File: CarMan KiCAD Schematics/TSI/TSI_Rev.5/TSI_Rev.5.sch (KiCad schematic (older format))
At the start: 24 parts, among them J25 Current_Sensor, J26 Conn_02x12_Counter_Clockwise

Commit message: TSI J13 & TSI J14
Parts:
- removed J?: J14, symbol Connector_Generic:Conn_01x04
- removed J?: J13, symbol Connector_Generic:Conn_01x04
- added J?: J14, symbol Connector_Generic:Conn_01x06
- added J?: J13, symbol Connector_Generic:Conn_01x02
- J?: value TSI J2 -> J2
- J?: value TSI J3 -> J3
- J?: value TSI J4 -> J4
- J?: value TSI J5 -> J5
- J?: value TSI J6 -> J6
- J?: value TSI J8 -> J8
- J?: value TSI J9 -> J9
- J?: value TSI J7 -> J7
- J?: value TSI J32 -> J32
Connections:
- net AMS_FAULT_LED: now also J?.1 (Pin_1)
- net FAULT_LED_RTN: now also J?.2 (Pin_2), J?.3 (Pin_3)
- net IMD_FAULT_LED: now also J?.4 (Pin_4)
- net TSAL: now also J?.1 (Pin_1)
- net TSAL_Cockpit: now also J?.5 (Pin_5)
- net TSAL_RTN: now also J?.2 (Pin_2), J?.6 (Pin_6)
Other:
- note added: "TSAL Roll \nHoop Power\n"
- note removed: "TSAL Power"
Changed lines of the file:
@@
 Text Label 9450 900  2    50   ~ 0
 AIRS
-Text Notes 7750 2100 0    50   ~ 0
+Text Notes 7800 2350 0    50   ~ 0
 Dashboard\n
-Text Label 7800 1650 2    50   ~ 0
-AMS_FAULT_LED
-Text Label 7800 1750 2    50   ~ 0
-FAULT_LED_RTN
-Text Label 7800 1950 2    50   ~ 0
-IMD_FAULT_LED
-Text Label 7800 1850 2    50   ~ 0
-FAULT_LED_RTN
 Text Notes 2450 1150 0    50   ~ 0
 Precharge Relay\n\n\n
@@
 Text Label 2500 1700 2    50   ~ 0
 GLV_RTN
-Text Notes 6750 2100 0    50   ~ 0
-TSAL Power
 Wire Wire Line
 	2750 4100 2850 4100
@@
 P 6000 900
 F 0 "J?" H 6080 892 50  0001 L CNN
-F 1 "TSI J2" H 5900 1250 50  0000 L CNN
+F 1 "J2" H 5950 1200 50  0000 L CNN
 F 2 "" H 6000 900 50  0001 C CNN
 F 3 "~" H 6000 900 50  0001 C CNN
@@
 P 6850 900
 F 0 "J?" H 6930 892 50  0001 L CNN
-F 1 "TSI J3" H 6750 1250 50  0000 L CNN
+F 1 "J3" H 6800 1200 50  0000 L CNN
 F 2 "" H 6850 900 50  0001 C CNN
 F 3 "~" H 6850 900 50  0001 C CNN
@@
 P 8950 900
 F 0 "J?" H 9030 892 50  0001 L CNN
-F 1 "TSI J5" H 8850 1250 50  0000 L CNN
+F 1 "J5" H 8900 1200 50  0000 L CNN
 F 2 "" H 8950 900 50  0001 C CNN
 F 3 "~" H 8950 900 50  0001 C CNN
@@
 Text Notes 8850 1500 0    50   ~ 0
 Testing\nConnector\n\n
-$Comp
-L Connector_Generic:Conn_01x04 J?
-U 1 1 5FE96F39
-P 9650 800
-F 0 "J?" H 9730 792 50  0001 L CNN
-F 1 "TSI J6" H 9550 1050 50  0000 L CNN
-F 2 "" H 9650 800 50  0001 C CNN
-F 3 "~" H 9650 800 50  0001 C CNN
-	1    9650 800
-	1    0    0    -1
-$EndComp
 $Comp
 L Connector_Generic:Conn_01x02 J?
@@
 P 2750 750
 F 0 "J?" H 2830 742 50  0001 L CNN
-F 1 "TSI J9" H 2650 900 50  0000 L CNN
+F 1 "J9" H 2700 850 50  0000 L CNN
 F 2 "" H 2750 750 50  0001 C CNN
 F 3 "~" H 2750 750 50  0001 C CNN
@@
 $Comp
 L Connector_Generic:Conn_01x04 J?
-U 1 1 600AD6CD
-P 8000 1750
-F 0 "J?" H 8080 1742 50  0001 L CNN
-F 1 "J14" H 7950 1950 50  0000 L CNN
-F 2 "" H 8000 1750 50  0001 C CNN
-F 3 "~" H 8000 1750 50  0001 C CNN
-	1    8000 1750
-	1    0    0    -1
-$EndComp
-$Comp
-L Connector_Generic:Conn_01x04 J?
 U 1 1 60109F6F
 P 9150 1800
 F 0 "J?" H 9230 1792 50  0001 L CNN
-F 1 "J15" H 9000 2050 50  0000 L CNN
+F 1 "J15" H 9050 2000 50  0000 L CNN
 F 2 "" H 9150 1800 50  0001 C CNN
 F 3 "~" H 9150 1800 50  0001 C CNN
@@
 P 1850 750
 F 0 "J?" H 1930 742 50  0001 L CNN
-F 1 "TSI J8" H 1750 900 50  0000 L CNN
+F 1 "J8" H 1800 850 50  0000 L CNN
 F 2 "" H 1850 750 50  0001 C CNN
 F 3 "~" H 1850 750 50  0001 C CNN
@@
 P 9950 1700
 F 0 "J?" H 10030 1692 50  0001 L CNN
-F 1 "J16" H 9850 1850 50  0000 L CNN
+F 1 "J16" H 9900 1800 50  0000 L CNN
 F 2 "" H 9950 1700 50  0001 C CNN
 F 3 "~" H 9950 1700 50  0001 C CNN
@@
 P 2750 2550
 F 0 "J?" H 2830 2542 50  0001 L CNN
-F 1 "J24" H 2650 2800 50  0000 L CNN
+F 1 "J24" H 2700 2750 50  0000 L CNN
 F 2 "" H 2750 2550 50  0001 C CNN
 F 3 "~" H 2750 2550 50  0001 C CNN
@@
 P 2700 1800
 F 0 "J?" H 2750 2117 50  0001 C CNN
-F 1 "TSI J7" H 2750 2025 50  0000 C CNN
+F 1 "J7" H 2750 2000 50  0000 C CNN
 F 2 "" H 2700 1800 50  0001 C CNN
 F 3 "~" H 2700 1800 50  0001 C CNN
@@
 AR Path="/6068B997" Ref="J?"  Part="1"
 F 0 "J?" H 3750 1117 50  0001 C CNN
-F 1 "TSI J32" H 3750 1025 50  0000 C CNN
+F 1 "J32" H 3750 1000 50  0000 C CNN
 F 2 "" H 3700 800 50  0001 C CNN
 F 3 "~" H 3700 800 50  0001 C CNN
@@
 Wire Wire Line
 	5100 800  5100 900
-$Comp
-L Connector_Generic:Conn_01x04 J?
-U 1 1 60794552
-P 6950 1750
-F 0 "J?" H 7030 1742 50  0001 L CNN
-F 1 "J13" H 6900 1950 50  0000 L CNN
-F 2 "" H 6950 1750 50  0001 C CNN
-F 3 "~" H 6950 1750 50  0001 C CNN
-	1    6950 1750
-	1    0    0    -1
-$EndComp
-Text Label 6750 1650 2    50   ~ 0
+Text Label 6750 1750 2    50   ~ 0
 TSAL
-Text Label 6750 1750 2    50   ~ 0
+Text Label 6750 1850 2    50   ~ 0
 TSAL_RTN
-Text Label 6750 1850 2    50   ~ 0
+Text Label 7900 2100 2    50   ~ 0
 TSAL_Cockpit
-Text Label 6750 1950 2    50   ~ 0
+Text Label 7900 2200 2    50   ~ 0
 TSAL_RTN
 Wire Wire Line
@@
 P 3650 2450
 F 0 "J?" H 3730 2442 50  0001 L CNN
-F 1 "J17" H 3550 2600 50  0000 L CNN
+F 1 "J17" H 3600 2550 50  0000 L CNN
 F 2 "" H 3650 2450 50  0001 C CNN
 F 3 "~" H 3650 2450 50  0001 C CNN
@@
 U 1 1 5FA6A834
 P 6950 3200
-F 0 "J26" H 7000 3917 50  0000 C CNN
-F 1 "Conn_02x12_Counter_Clockwise" H 7000 3826 50  0000 C CNN
+F 0 "J26" H 7000 3800 50  0000 C CNN
+F 1 "Conn_02x12_Counter_Clockwise" H 7000 3826 50  0001 C CNN
 F 2 "" H 6950 3200 50  0001 C CNN
 F 3 "~" H 6950 3200 50  0001 C CNN
@@
 P 8000 700
 F 0 "J?" H 8080 692 50  0001 L CNN
-F 1 "TSI J4" H 7900 850 50  0000 L CNN
+F 1 "J4" H 7950 800 50  0000 L CNN
 F 2 "" H 8000 700 50  0001 C CNN
 F 3 "~" H 8000 700 50  0001 C CNN
@@
 Text Notes 2100 1400 0    89   ~ 18
 High Voltage Connectors
+Text Notes 6800 2100 0    50   ~ 0
+TSAL Roll \nHoop Power\n
+$Comp
+L Connector_Generic:Conn_01x06 J?
+U 1 1 5FA1229F
+P 8100 1900
+F 0 "J?" H 8180 1892 50  0001 L CNN
+F 1 "J14" H 8050 2200 50  0000 L CNN
+F 2 "" H 8100 1900 50  0001 C CNN
+F 3 "~" H 8100 1900 50  0001 C CNN
+	1    8100 1900
+	1    0    0    -1
+$EndComp
+Text Label 7900 1900 2    50   ~ 0
+FAULT_LED_RTN
+Text Label 7900 2000 2    50   ~ 0
+IMD_FAULT_LED
+Text Label 7900 1800 2    50   ~ 0
+FAULT_LED_RTN
+Text Label 7900 1700 2    50   ~ 0
+AMS_FAULT_LED
+$Comp
+L Connector_Generic:Conn_01x02 J?
+U 1 1 5FA5AE22
+P 6950 1750
+F 0 "J?" H 7030 1742 50  0001 L CNN
+F 1 "J13" H 6900 1850 50  0000 L CNN
+F 2 "" H 6950 1750 50  0001 C CNN
+F 3 "~" H 6950 1750 50  0001 C CNN
+	1    6950 1750
+	1    0    0    -1
+$EndComp
+$Comp
+L Connector_Generic:Conn_01x04 J?
+U 1 1 5FE96F39
+P 9650 800
+F 0 "J?" H 9730 792 50  0001 L CNN
+F 1 "J6" H 9600 1000 50  0000 L CNN
+F 2 "" H 9650 800 50  0001 C CNN
+F 3 "~" H 9650 800 50  0001 C CNN
+	1    9650 800
+	1    0    0    -1
+$EndComp
 $EndSCHEMATC

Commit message: NO J12
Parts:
- removed J?: J12, symbol Connector_Generic:Conn_01x04
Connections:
- no-connect marks 11 -> 10
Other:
- note removed: "Cooling\nControl\n\n"
- note removed: "I2C Connection \nbetween Logic & TSI\n\n"
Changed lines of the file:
@@
 Comment4 ""
 $EndDescr
-Text Label 5800 1850 2    50   ~ 0
-GPIO_I2C_RTN
 Text Label 5800 700  2    50   ~ 0
 Flowrate
@@
 Text Notes 1050 1150 2    50   ~ 0
 HV
-Text Notes 5850 1500 0    50   ~ 0
-Cooling\nControl\n\n
 Text Label 9450 700  2    50   ~ 0
 SL1_Out
@@
 $Comp
 L Connector_Generic:Conn_01x04 J?
-U 1 1 5FFF16D2
-P 6000 1750
-F 0 "J?" H 6080 1742 50  0001 L CNN
-F 1 "J12" H 5950 1950 50  0000 L CNN
-F 2 "" H 6000 1750 50  0001 C CNN
-F 3 "~" H 6000 1750 50  0001 C CNN
-	1    6000 1750
-	1    0    0    -1
-$EndComp
-Text Notes 5650 2250 0    50   ~ 0
-I2C Connection \nbetween Logic & TSI\n\n
-Text Label 5800 1650 2    50   ~ 0
-SDA
-Text Label 5800 1750 2    50   ~ 0
-SCL
-NoConn ~ 5800 1950
-$Comp
-L Connector_Generic:Conn_01x04 J?

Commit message: Update
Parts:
- J?: value TSI J20 -> J20
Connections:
- net Break_Pressed_uC is gone; now on net Brake_Pressed_uC: J26.10 (Pin_10)
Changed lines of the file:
@@
 IMD_Status_3.3
 Text Label 6750 3600 2    50   ~ 0
-Break_Pressed_uC
+Brake_Pressed_uC
 Text Label 6750 3700 2    50   ~ 0
 APPS
@@
 P 10950 1900
 F 0 "J?" H 11030 1892 50  0001 L CNN
-F 1 "TSI J20" H 10850 2250 50  0000 L CNN
+F 1 "J20" H 10900 2200 50  0000 L CNN
 F 2 "" H 10950 1900 50  0001 C CNN
 F 3 "~" H 10950 1900 50  0001 C CNN

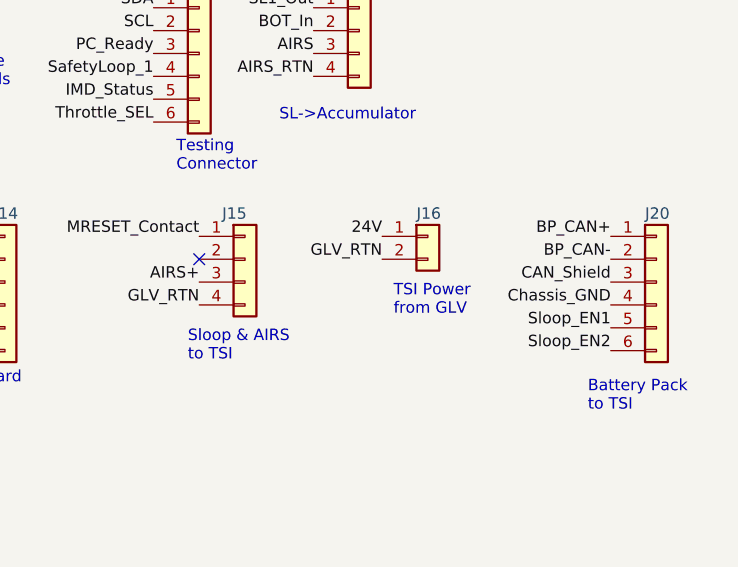
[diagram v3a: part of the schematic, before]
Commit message: J16 - Added added SL1_In
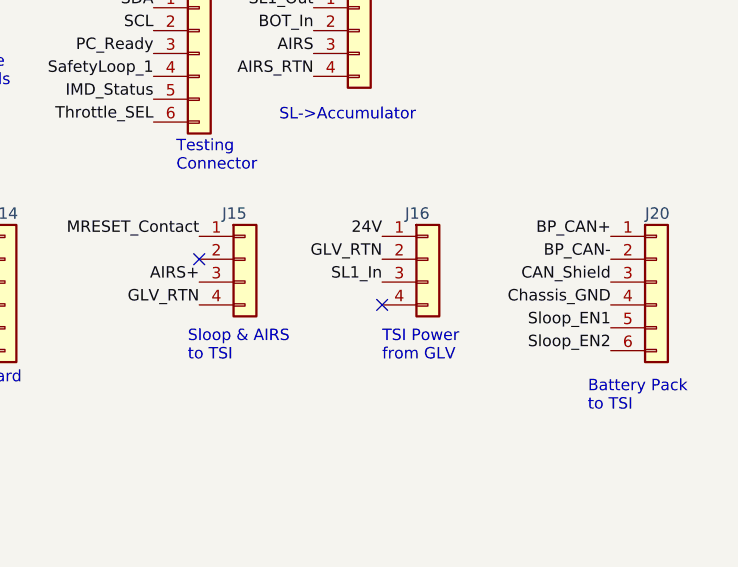
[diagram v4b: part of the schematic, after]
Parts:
- removed J?: J16, symbol Connector_Generic:Conn_01x02
- added J?: J16, symbol Connector_Generic:Conn_01x04
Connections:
- net 24V: now also J?.1 (Pin_1)
- net FAULT_LED_RTN: now also J?.2 (Pin_2)
- net SL1_In: now also J?.3 (Pin_3)
- no-connect marks 10 -> 11
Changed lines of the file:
@@
 Text Label 8950 1900 2    50   ~ 0
 AIRS+
-Text Notes 9800 2050 0    50   ~ 0
+Text Notes 9750 2250 0    50   ~ 0
 TSI Power \nfrom GLV\n
-Text Label 9750 1700 2    50   ~ 0
-24V
-Text Label 9750 1800 2    50   ~ 0
-GLV_RTN
 Wire Wire Line
 	2750 3400 2850 3400
@@
 Discharge Relay
 $Comp
-L Connector_Generic:Conn_01x02 J?
-U 1 1 60187F86
-P 9950 1700
-F 0 "J?" H 10030 1692 50  0001 L CNN
-F 1 "J16" H 9900 1800 50  0000 L CNN
-F 2 "" H 9950 1700 50  0001 C CNN
-F 3 "~" H 9950 1700 50  0001 C CNN
-	1    9950 1700
-	1    0    0    -1
-$EndComp
-$Comp
 L Connector_Generic:Conn_01x04 J?
 U 1 1 601D2101
@@
 	1    0    0    -1
 $EndComp
+$Comp
+L Connector_Generic:Conn_01x04 J?
+U 1 1 5FAB288F
+P 9950 1800
+F 0 "J?" H 10030 1792 50  0001 L CNN
+F 1 "J16" H 9850 2000 50  0000 L CNN
+F 2 "" H 9950 1800 50  0001 C CNN
+F 3 "~" H 9950 1800 50  0001 C CNN
+	1    9950 1800
+	1    0    0    -1
+$EndComp
+NoConn ~ 9750 2000
+Text Label 9750 1700 2    50   ~ 0
+24V
+Text Label 9750 1800 2    50   ~ 0
+GLV_RTN
+Text Label 9750 1900 2    50   ~ 0
+SL1_In
 $EndSCHEMATC

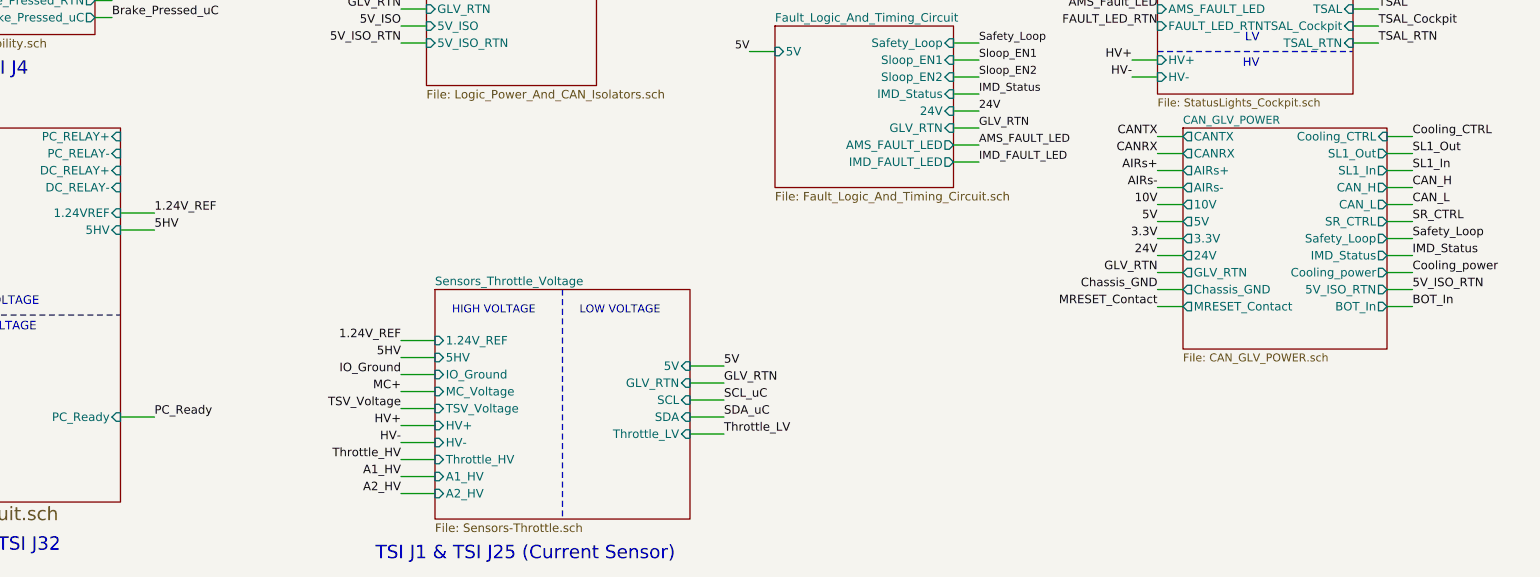
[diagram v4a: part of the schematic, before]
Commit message: Removed CAN Transciever from CAN & GLV Power, edited net listing on PCDC Circuit regarding Safety_Loop Iso and extraneous connector
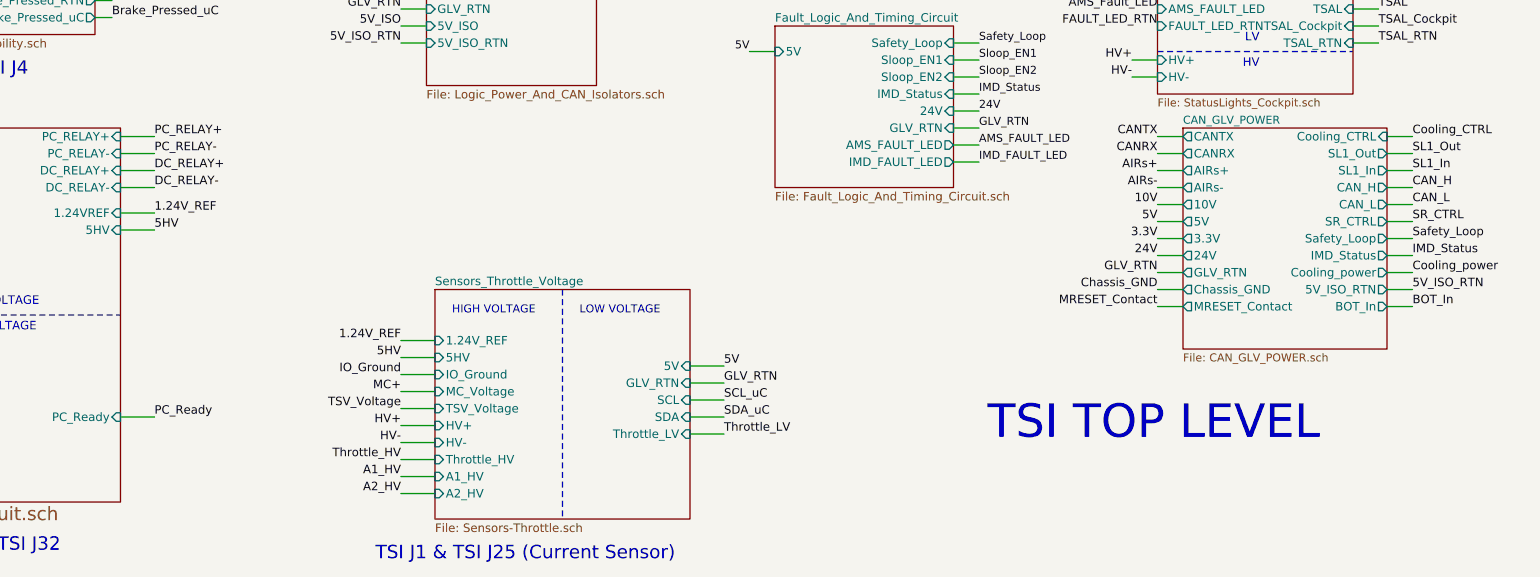
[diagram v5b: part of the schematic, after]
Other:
- note added: "TSI TOP LEVEL\n"
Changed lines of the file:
@@
 Text Label 9750 1900 2    50   ~ 0
 SL1_In
+Text Notes 8000 7000 0    197  ~ 0
+TSI TOP LEVEL\n
+Wire Wire Line
+	3100 5400 2900 5400
+Wire Wire Line
+	3100 5500 2900 5500
+Wire Wire Line
+	3100 5200 2900 5200
+Wire Wire Line
+	3100 5300 2900 5300
+Text Label 3100 5200 0    50   ~ 0
+PC_RELAY+
+Text Label 3100 5300 0    50   ~ 0
+PC_RELAY-
+Text Label 3100 5400 0    50   ~ 0
+DC_RELAY+
+Text Label 3100 5500 0    50   ~ 0
+DC_RELAY-
 $EndSCHEMATC

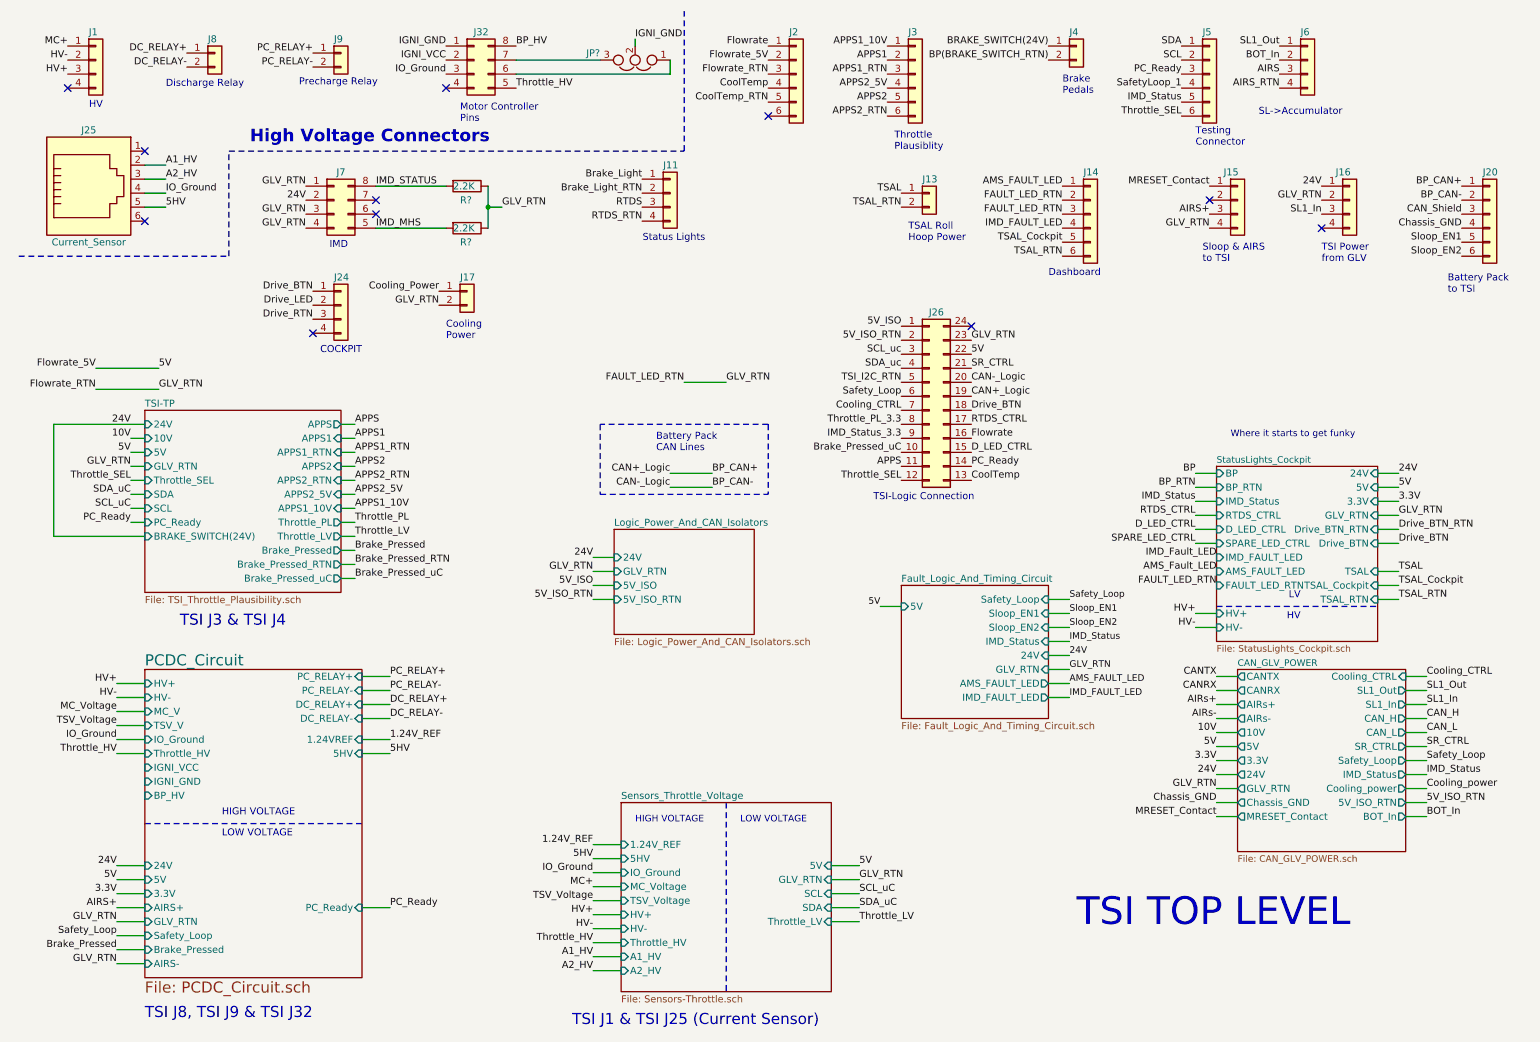
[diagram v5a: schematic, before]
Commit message: BP_HV - > Brake_Pressed_HV net list changes
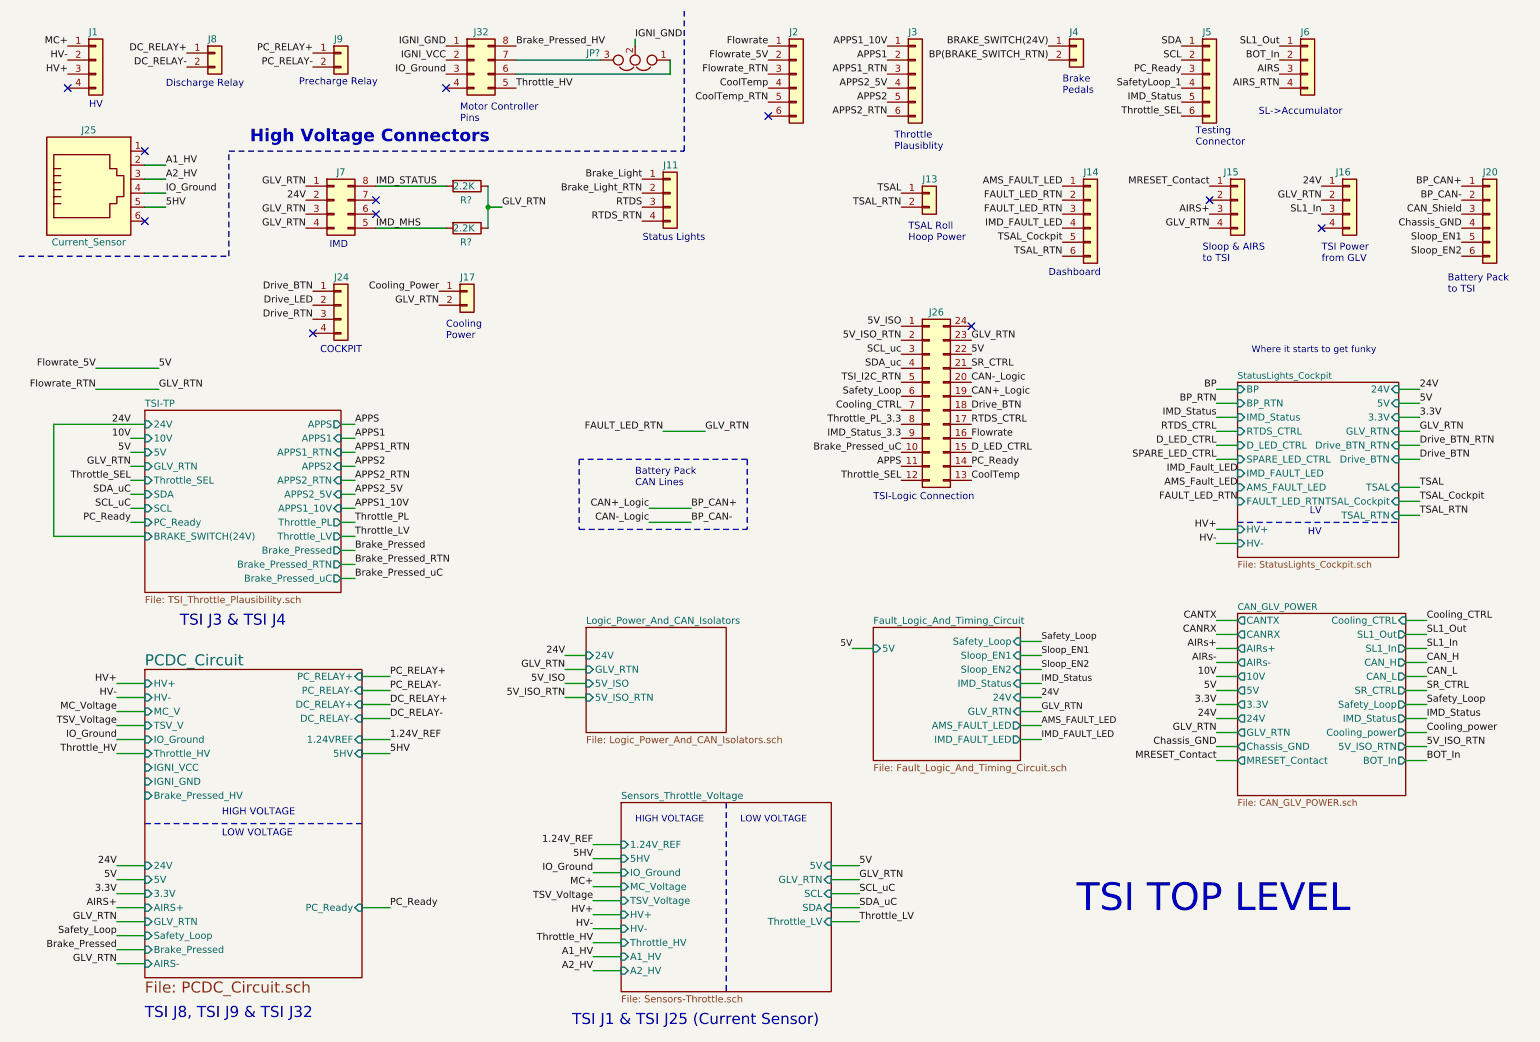
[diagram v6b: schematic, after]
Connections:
- net BP_HV renamed Brake_Pressed_HV
